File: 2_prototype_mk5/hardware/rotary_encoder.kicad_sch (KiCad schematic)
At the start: 2 parts, among them J7 Conn_01x05, SW3 PEC12R-2120F-S0012

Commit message: MKV revision 1
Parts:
- J7: LCSC Part Number (none) -> C124379; LCSC_Part_Number C124379 -> (none)
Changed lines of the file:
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@@
-			)
-		)
-		(property "LCSC_Part_Number" ""
-			(at 146.05 77.47 0)
-			(hide yes)
-			(show_name no)
-			(do_not_autoplace no)
-			(effects
-				(font
-					(size 1.27 1.27)
-				)
 			)
 		)
@@
 			)
 		)
-		(property "LCSC_Part_Number" "C124379"
-			(at 201.93 82.55 0)
-			(hide yes)
+		(property "LCSC Part Number" "C124379"
+			(at 201.93 82.55 0)
+			(hide yes)

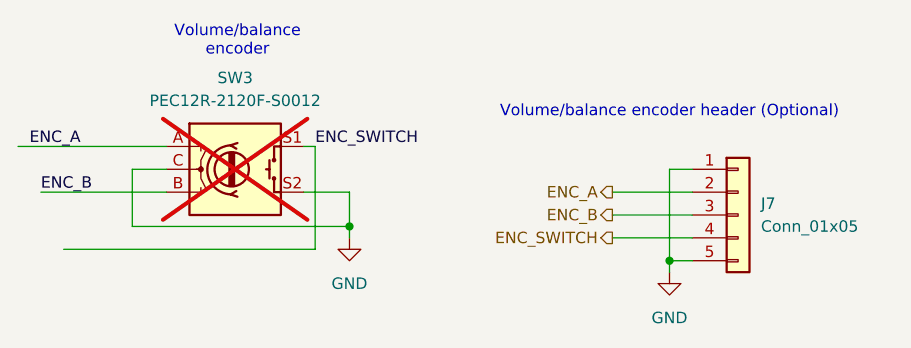
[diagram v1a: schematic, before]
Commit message: Cost reductions for JCLPCB
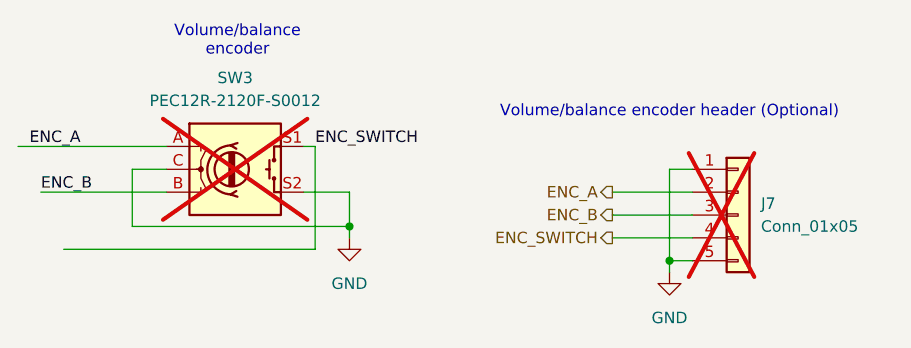
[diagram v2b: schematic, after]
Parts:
- J7: now not fitted; now left out of the parts list
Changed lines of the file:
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@@
 		(body_style 1)
 		(exclude_from_sim no)
-		(in_bom yes)
+		(in_bom no)
 		(on_board yes)
 		(in_pos_files yes)
-		(dnp no)
+		(dnp yes)
 		(fields_autoplaced yes)
 		(property "Reference" "J7"
